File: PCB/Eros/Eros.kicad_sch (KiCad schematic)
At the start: 76 parts, among them J1 USB_C_PowerOnly_6P, J2 UART, J3 Li-ion, J5 JST_SPI_SCREEN, J6 Micro_SD_Card, Q1 BC817, SW1 SW_Push, SW2 SW_Push, SW3 SW_Push, SW4 SW_Push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

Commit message: Add dnp filter resistors/capacitor
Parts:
- added C26, C27: C, Capacitor_SMD:C_0402_1005Metric_Pad0.74x0.62mm_HandSolder, symbol Device:C
- added R29, R30: R, Resistor_SMD:R_0402_1005Metric_Pad0.72x0.64mm_HandSolder, symbol Device:R
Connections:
- net GND: now also C27.1, R29.2
- net REFIN: now also C27.2, R29.1
- net REFOUT: now also C26.2
- net SW: now also C26.1, R30.1
- net at R24.2, R25.1, R26.2: now also R30.2
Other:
- note added: "ECG MODULE"
- note removed: "EKG MODULE"
- moved on the sheet: C23, C25, R28, U5

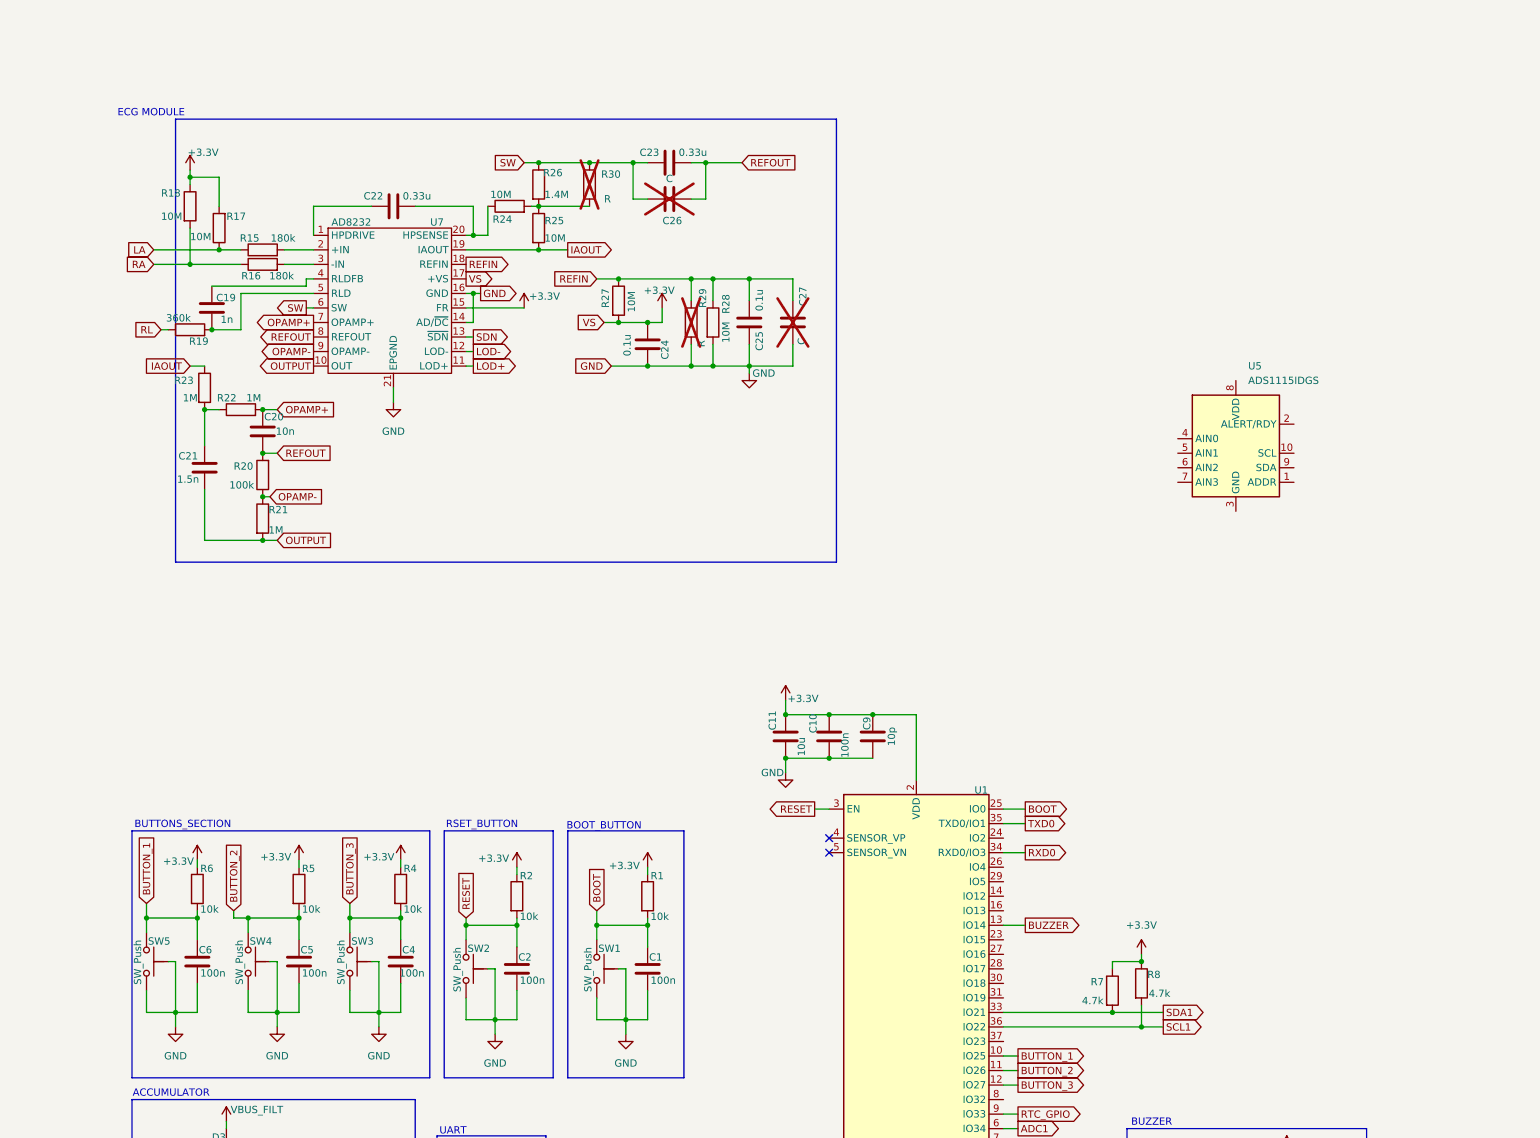
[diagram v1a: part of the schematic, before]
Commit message: wire ads1115
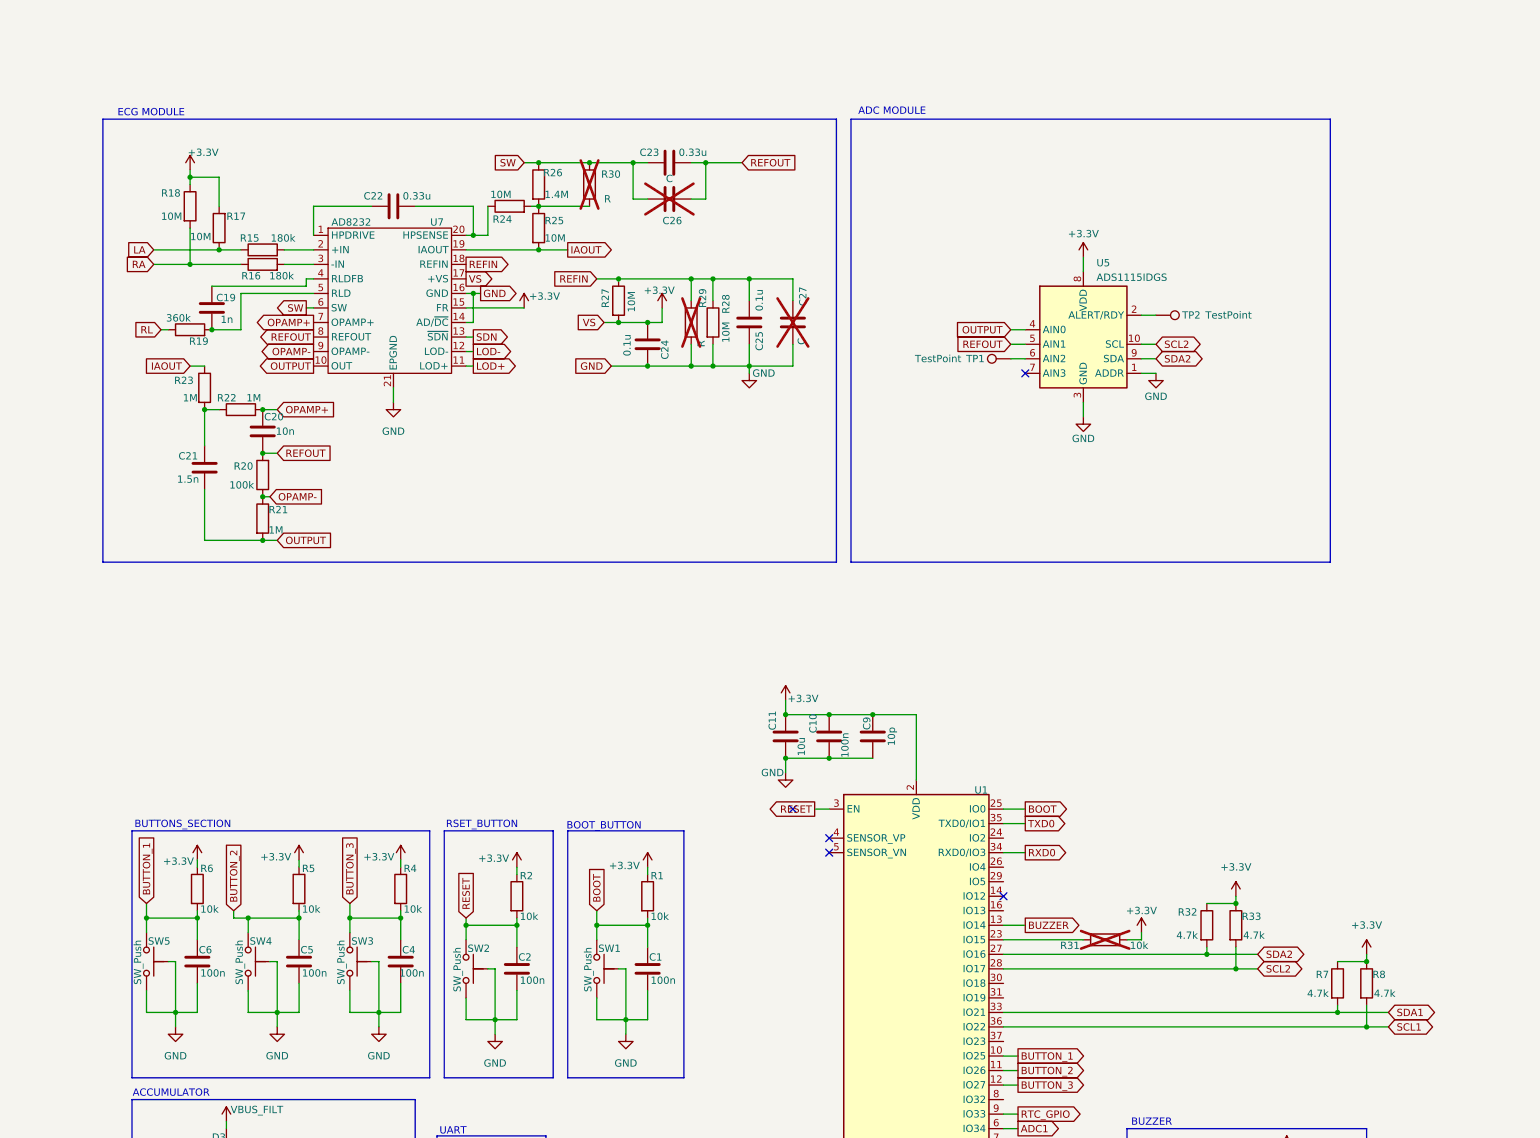
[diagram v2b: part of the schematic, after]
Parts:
- added R31: 10k, Resistor_SMD:R_0402_1005Metric_Pad0.72x0.64mm_HandSolder, symbol Device:R
- added R32, R33: 4.7k, Resistor_SMD:R_0402_1005Metric, symbol Device:R
- added TP1, TP2: TestPoint, TestPoint:TestPoint_Pad_D1.5mm, symbol Connector:TestPoint
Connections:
- net +3.3V: now also U5.8 (VDD), R31.1, R32.1, R33.1
- net GND: now also U5.1 (ADDR), U5.3 (GND)
- net OUTPUT: now also U5.4 (AIN0)
- net REFOUT: now also U5.5 (AIN1)
- net SCL2: now reaches U5.10 (SCL)
- net SCL2: now also U1.28 (IO17), R33.2
- net at U5.2 (ALERT/RDY): now also TP2.1
- net at U5.6 (AIN2): now also TP1.1
- net SDA2: now reaches U5.9 (SDA)
- net SDA2: now also U1.27 (IO16), R32.2
- net at U1.23 (IO15): now also R31.2
- no-connect marks 7 -> 10
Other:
- note added: "ADC MODULE"
- moved on the sheet: R7, R8, U5

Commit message: ad TPs, align boxes
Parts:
- removed J5: JST_SPI_SCREEN, Connector_JST:JST_PH_S4B-PH-K_1x04_P2.00mm_Horizontal, symbol Connector:Conn_01x04_Pin
- added J4: Conn_01x08_Socket, symbol Connector:Conn_01x08_Socket
- added TP1, TP2, TP3, TP4: TestPoint, TestPoint:TestPoint_Pad_D1.5mm, symbol Connector:TestPoint
- renumbered TP1 to TP10, TP2 to TP11
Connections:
- net +3.3V: now also TP4.1
- net Acc: now also TP3.1
- net GND: now also J6.9 (SHIELD), TP1.1
- net VBUS_FILT: now also TP2.1
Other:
- note added: "MICROSD SLOT"
- note added: "RESET_BUTTON"
- note added: "SPI SCREEN"
- note added: "TEST PADS AND CONNECTIONS"
- note removed: "RSET_BUTTON"
- moved on the sheet: Buzzer1, C10, C11, C3, C7, C8, C9, D2, J2, J6, Q1, R13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

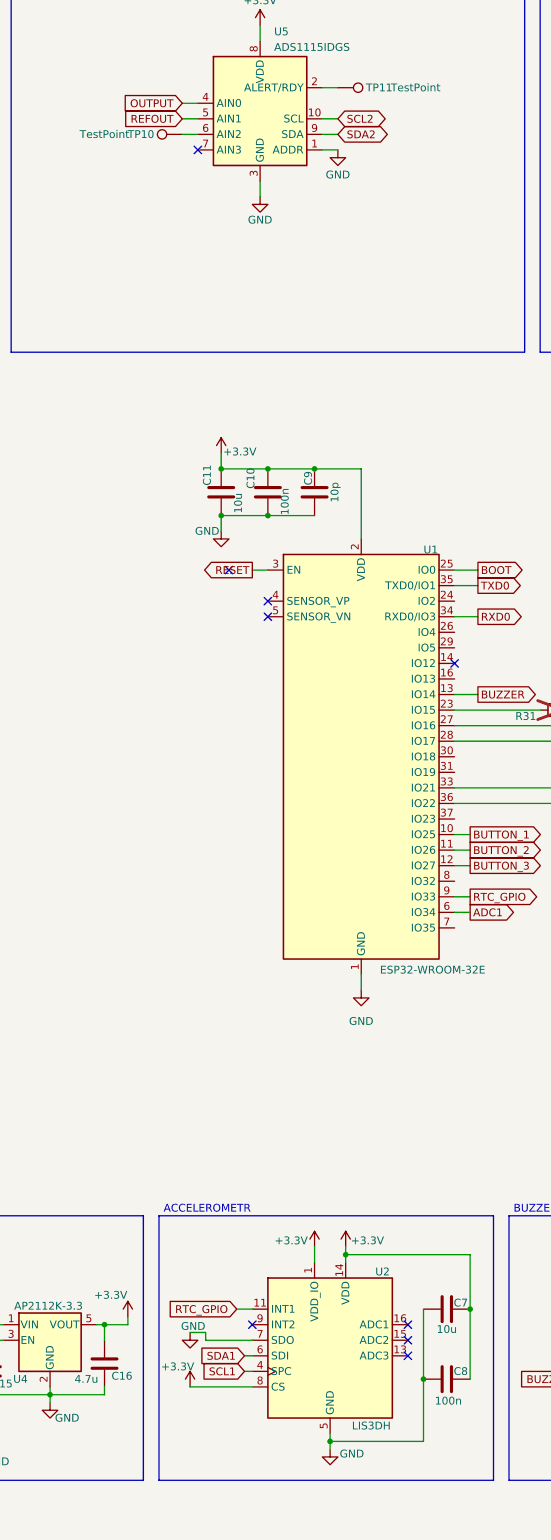
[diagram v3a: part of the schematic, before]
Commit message: change I2C labels
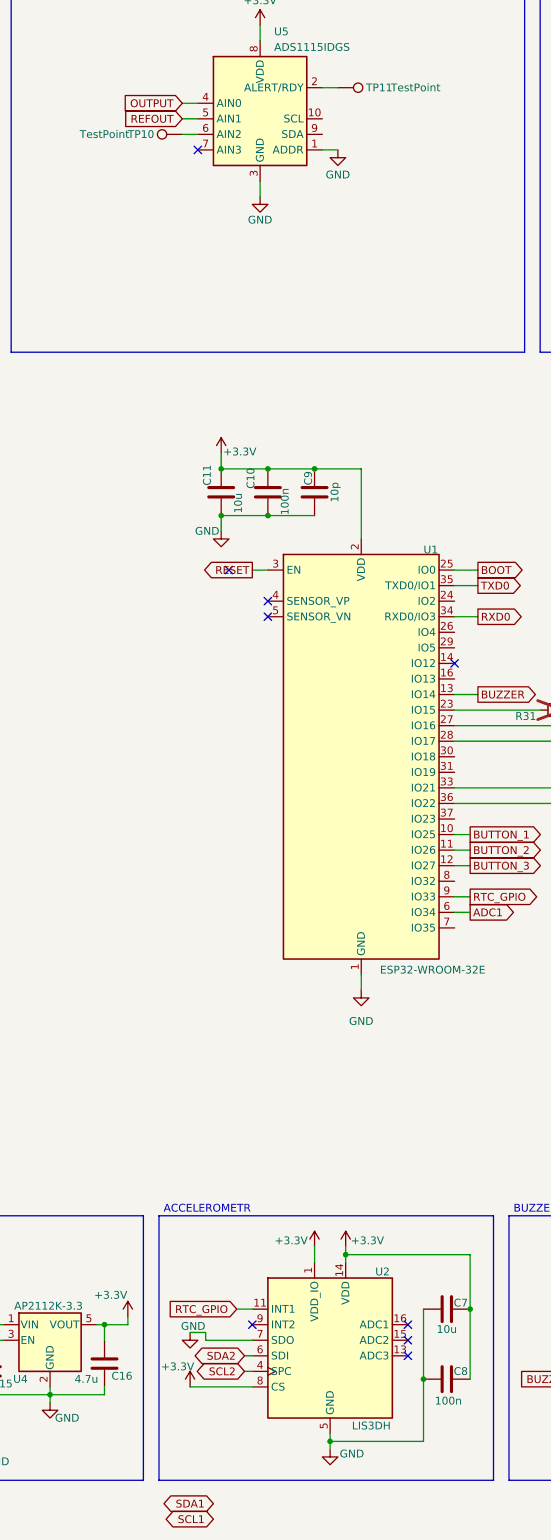
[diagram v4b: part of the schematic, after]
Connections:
- net SCL1: no longer U2.4 (SPC)
- net SCL2: now also U2.4 (SPC); no longer U5.10 (SCL)
- net SDA1: no longer U2.6 (SDI)
- net SDA2: now also U2.6 (SDI); no longer U5.9 (SDA)
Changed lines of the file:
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@@
-	(wire
-		(pts
-			(xy 195.58 54.61) (xy 198.12 54.61)
-		)
-		(stroke
-			(width 0)
-			(type default)
-		)
-	)
 	(wire
 		(pts
@@
 		(pts
 			(xy 179.07 119.38) (xy 179.07 121.92)
-		)
-		(stroke
-			(width 0)
-			(type default)
-		)
-	)
-	(wire
-		(pts
-			(xy 195.58 57.15) (xy 198.12 57.15)
 		)
 		(stroke
@@
 		)
 	)
-	(global_label "SCL1"
-		(shape input)
-		(at 182.88 259.08 180)
-		(fields_autoplaced yes)
-		(effects
-			(font
-				(size 1.27 1.27)
-			)
-			(justify right)
-		)
-		(property "Intersheetrefs" "${INTERSHEET_REFS}"
-			(at 175.1777 259.08 0)
-			(effects
-				(font
-					(size 1.27 1.27)
-				)
-				(justify right)
-				(hide yes)
-			)
-		)
-	)
 	(global_label "SCL2"
 		(shape bidirectional)
@@
 		)
 	)
+	(global_label "SDA1"
+		(shape bidirectional)
+		(at 177.8 280.67 180)
+		(fields_autoplaced yes)
+		(effects
+			(font
+				(size 1.27 1.27)
+			)
+			(justify right)
+		)
+		(property "Intersheetrefs" "${INTERSHEET_REFS}"
+			(at 168.9259 280.67 0)
+			(effects
+				(font
+					(size 1.27 1.27)
+				)
+				(justify right)
+				(hide yes)
+			)
+		)
+	)
 	(global_label "BOOT"
 		(shape input)
@@
 		)
 	)
-	(global_label "SDA2"
-		(shape bidirectional)
-		(at 198.12 57.15 0)
-		(fields_autoplaced yes)
-		(effects
-			(font
-				(size 1.27 1.27)
-			)
-			(justify left)
-		)
-		(property "Intersheetrefs" "${INTERSHEET_REFS}"
-			(at 206.9941 57.15 0)
-			(effects
-				(font
-					(size 1.27 1.27)
-				)
-				(justify left)
-				(hide yes)
-			)
-		)
-	)
 	(global_label "ADC1"
 		(shape input)
@@
 		)
 	)
-	(global_label "SCL2"
+	(global_label "SCL1"
 		(shape bidirectional)
-		(at 198.12 54.61 0)
-		(fields_autoplaced yes)
-		(effects
-			(font
-				(size 1.27 1.27)
-			)
-			(justify left)
-		)
-		(property "Intersheetrefs" "${INTERSHEET_REFS}"
-			(at 206.9336 54.61 0)
-			(effects
-				(font
-					(size 1.27 1.27)
-				)
-				(justify left)
+		(at 177.8 283.21 180)
+		(fields_autoplaced yes)
+		(effects
+			(font
+				(size 1.27 1.27)
+			)
+			(justify right)
+		)
+		(property "Intersheetrefs" "${INTERSHEET_REFS}"
+			(at 168.9864 283.21 0)
+			(effects
+				(font
+					(size 1.27 1.27)
+				)
+				(justify right)
 				(hide yes)
 			)
@@
 		)
 	)
-	(global_label "SDA1"
-		(shape input)
+	(global_label "SDA2"
+		(shape bidirectional)
 		(at 182.88 256.54 180)
 		(fields_autoplaced yes)
@@
 		)
 		(property "Intersheetrefs" "${INTERSHEET_REFS}"
-			(at 175.1172 256.54 0)
+			(at 174.0059 256.54 0)
 			(effects
 				(font
@@
 				(hide yes)
 			)
+		)
+	)
+	(global_label "SCL2"
+		(shape bidirectional)
+		(at 182.88 259.08 180)
+		(fields_autoplaced yes)
+		(effects
+			(font
+				(size 1.27 1.27)
+			)
+			(justify right)
+		)
+		(property "Intersheetrefs" "${INTERSHEET_REFS}"
+			(at 174.0664 259.08 0)
+			(effects
+				(font
+					(size 1.27 1.27)
+				)
+				(justify right)
+				(hide yes)
+			)
